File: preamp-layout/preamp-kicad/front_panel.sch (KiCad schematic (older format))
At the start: 30 parts, among them J16 Conn_01x03_Female, J17 Conn_01x03_Female, J18 Conn_01x03_Female, J19 Conn_01x03_Female, J20 Conn_01x03_Female, J21 Conn_01x03_Female, J22 Conn_01x03_Female, J23 Conn_01x03_Female, J24 Conn_01x05_Female, J25 Conn_01x02_Male, J26 Conn_01x02_Male, U4 MC33978

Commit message: Conn / Pin Updates
Updated cable headers, pin names, MCU conn layout. MCP4902 changeout for custom symbol.
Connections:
- net labels added: ~CS
- net labels removed: CS
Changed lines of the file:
@@
 CLK
 Text HLabel 6050 3400 0    50   Input ~ 0
-CS
+~CS
 Wire Wire Line
 	6050 3200 6200 3200
@@
 	1    0    0    -1
 $EndComp
-Text HLabel 9550 1650 0    50   Output ~ 0
+Text HLabel 9550 1750 0    50   Output ~ 0
 MISO
+Text HLabel 9550 1550 0    50   Input ~ 0
+CLK
+Text HLabel 9550 1650 0    50   Input ~ 0
+MOSI
 Text HLabel 9550 1450 0    50   Input ~ 0
-CLK
-Text HLabel 9550 1550 0    50   Input ~ 0
-MOSI
-Text HLabel 9550 1750 0    50   Input ~ 0
-CS
+~CS
 Text HLabel 9550 1850 0    50   Output ~ 0
 SW_INT

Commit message: I2C init commit
Changed design from using SPI interface to I2C interface, with exception of front LED array (SPI).
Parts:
- removed U4: MC33978, symbol preamp:MC33978
- added R122, R123, R124, R125, R70, R71: 1k, Resistor_SMD:R_1206_3216Metric_Pad1.42x1.75mm_HandSolder, symbol Device:R
- added SW10, SW11: Rotary_Encoder_Switch, symbol Device:Rotary_Encoder_Switch
- added U4: MCP23017_SO, Package_SO:SOIC-28W_7.5x17.9mm_P1.27mm, symbol Interface_Expansion:MCP23017_SO
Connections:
- net labels added: FP_INTA, FP_INTB, FP_SCL, FP_SDA, SEL_CLK, SEL_DT, SEL_SW, VOL_CLK, VOL_DT, VOL_SW, ~FP_RST
- net labels removed: CLK, MISO, MOSI, SW_INT, ~CS
- wire segments 122 -> 172
- no-connect marks 16 -> 2
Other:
- moved on the sheet: C17, C18, C19, C20, C21, C22, C23, C24, D12, J16, J17, J18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

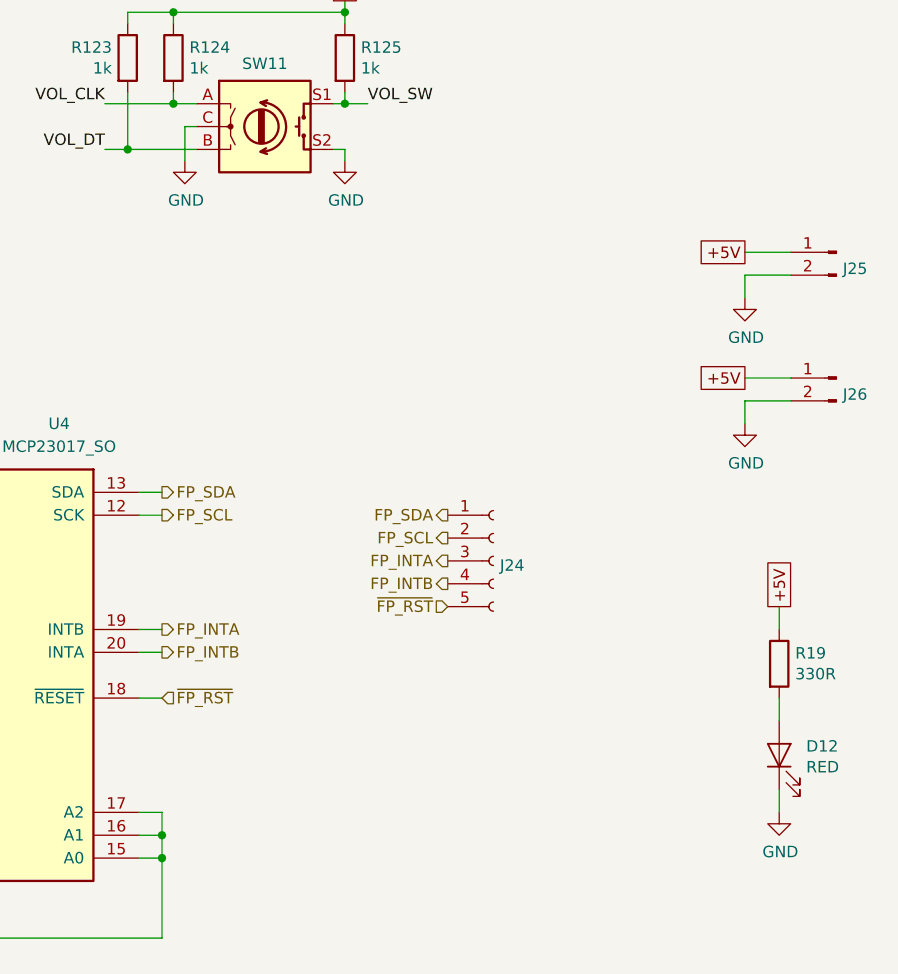
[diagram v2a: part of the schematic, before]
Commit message: Minor Updates
Moved headphone jack to amp pcb. I2C pin updates. Added caps to LED light strip. Added 0.1uF caps to all ICs.
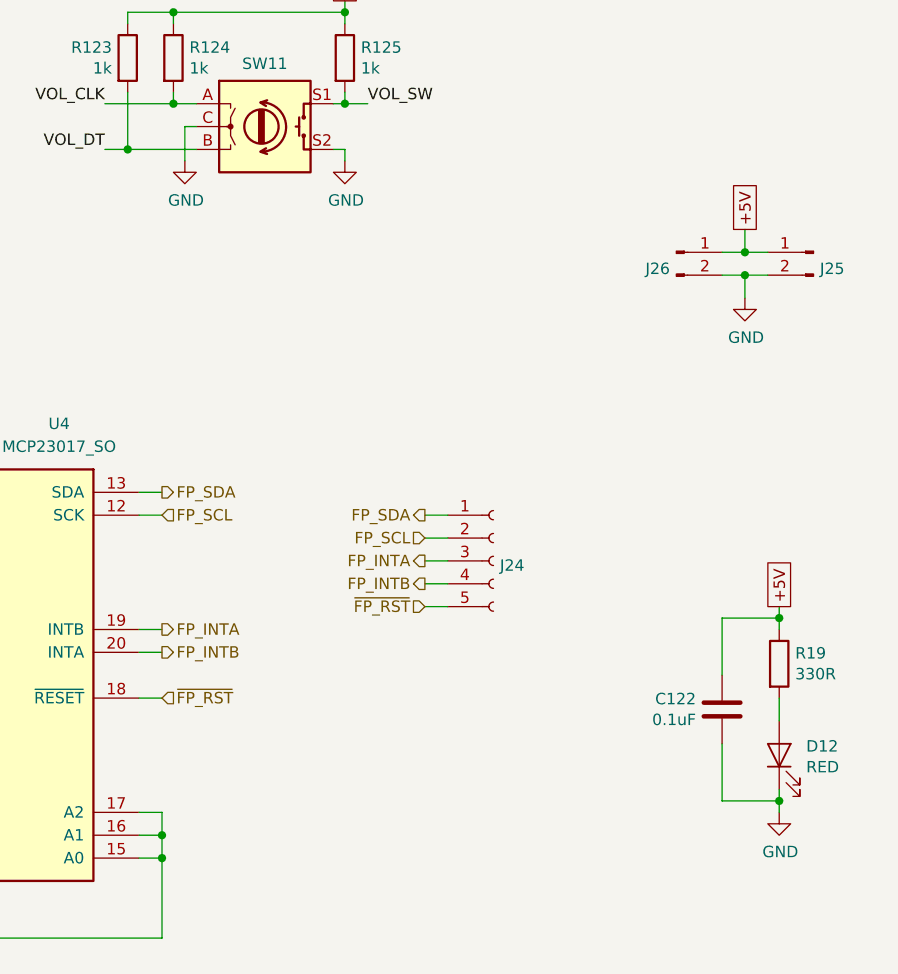
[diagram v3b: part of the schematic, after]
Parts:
- added C122: 0.1uF, Capacitor_SMD:C_0805_2012Metric_Pad1.15x1.40mm_HandSolder, symbol Device:C
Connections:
- net +5V: now also C122.1
- net GND: now also C122.2
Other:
- moved on the sheet: J25, J26
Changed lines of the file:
@@
 $Descr A4 11693 8268
 encoding utf-8
-Sheet 5 13
+Sheet 13 13
 Title "Front Panel"
 Date "2020-02-25"
@@
 $EndComp
 Wire Wire Line
-	10150 5050 10150 5150
+	10150 5050 10150 5100
 Wire Wire Line
 	10150 4650 10150 4750
 Wire Wire Line
-	10150 4250 10150 4350
+	10150 4250 10150 4300
 $Comp
 L Device:LED D?
@@
 L Connector:Conn_01x02_Male J?
 U 1 1 5E8B15E1
-P 10400 3250
+P 9700 2700
 AR Path="/5E5EF2D4/5E8B15E1" Ref="J?"  Part="1"
 AR Path="/6009D432/5E8B15E1" Ref="J?"  Part="1"
 AR Path="/5E5ECAAE/5E8B15E1" Ref="J26"  Part="1"
-F 0 "J26" H 10372 3178 50  0000 R CNN
-F 1 "Conn_01x02_Male" H 10372 3133 50  0001 R CNN
-F 2 "Connector_JST:JST_EH_B2B-EH-A_1x02_P2.50mm_Vertical" H 10400 3250 50  0001 C CNN
-F 3 "~" H 10400 3250 50  0001 C CNN
-	1    10400 3250
-	-1   0    0    -1
+F 0 "J26" H 9672 2628 50  0000 R CNN
+F 1 "Conn_01x02_Male" H 9672 2583 50  0001 R CNN
+F 2 "Connector_JST:JST_EH_B2B-EH-A_1x02_P2.50mm_Vertical" H 9700 2700 50  0001 C CNN
+F 3 "~" H 9700 2700 50  0001 C CNN
+	1    9700 2700
+	1    0    0    -1
 $EndComp
 $Comp
@@
 	1    0    0    -1
 $EndComp
-$Comp
-L power:GND #PWR?
-U 1 1 64EC55E1
-P 10000 3450
-AR Path="/5E26F6FE/64EC55E1" Ref="#PWR?"  Part="1"
-AR Path="/5E5ECAAE/64EC55E1" Ref="#PWR029"  Part="1"
-F 0 "#PWR029" H 10000 3200 50  0001 C CNN
-F 1 "GND" H 10005 3277 50  0000 C CNN
-F 2 "" H 10000 3450 50  0001 C CNN
-F 3 "" H 10000 3450 50  0001 C CNN
-	1    10000 3450
-	1    0    0    -1
-$EndComp
-Wire Wire Line
-	10200 3250 10000 3250
-Wire Wire Line
-	10000 3350 10000 3450
-Wire Wire Line
-	10200 3350 10000 3350
-Text GLabel 10000 3250 0    50   UnSpc ~ 0
-+5V
-Wire Wire Line
-	10200 2700 10000 2700
 Wire Wire Line
 	10000 2800 10000 2900
-Wire Wire Line
-	10200 2800 10000 2800
-Text GLabel 10000 2700 0    50   UnSpc ~ 0
+Text GLabel 10000 2600 1    50   UnSpc ~ 0
 +5V
 $Comp
 L Connector:Conn_01x02_Male J?
 U 1 1 60B80487
-P 10400 2700
+P 10300 2700
 AR Path="/5E5EF2D4/60B80487" Ref="J?"  Part="1"
 AR Path="/6009D432/60B80487" Ref="J?"  Part="1"
 AR Path="/5E5ECAAE/60B80487" Ref="J25"  Part="1"
-F 0 "J25" H 10372 2628 50  0000 R CNN
-F 1 "Conn_01x02_Male" H 10372 2583 50  0001 R CNN
-F 2 "Connector_JST:JST_EH_B2B-EH-A_1x02_P2.50mm_Vertical" H 10400 2700 50  0001 C CNN
-F 3 "~" H 10400 2700 50  0001 C CNN
-	1    10400 2700
+F 0 "J25" H 10272 2628 50  0000 R CNN
+F 1 "Conn_01x02_Male" H 10272 2583 50  0001 R CNN
+F 2 "Connector_JST:JST_EH_B2B-EH-A_1x02_P2.50mm_Vertical" H 10300 2700 50  0001 C CNN
+F 3 "~" H 10300 2700 50  0001 C CNN
+	1    10300 2700
 	-1   0    0    -1
 $EndComp
@@
 	6650 5650 6650 5700
 Wire Wire Line
-	6650 3350 6650 3450
-Wire Wire Line
 	7350 5150 7450 5150
 Wire Wire Line
@@
 	1    0    0    -1
 $EndComp
-Text HLabel 8700 4150 0    50   Output ~ 0
+Text HLabel 8600 4150 0    50   Output ~ 0
 FP_INTB
-Text HLabel 8700 3950 0    50   Output ~ 0
-FP_SCL
-Text HLabel 8700 4050 0    50   Output ~ 0
+Text HLabel 8600 4050 0    50   Output ~ 0
 FP_INTA
-Text HLabel 8700 3850 0    50   Output ~ 0
-FP_SDA
-Text HLabel 8700 4250 0    50   Input ~ 0
+Text HLabel 8600 4250 0    50   Input ~ 0
 ~FP_RST
 Text HLabel 7450 4450 2    50   Output ~ 0
 FP_INTB
-Text HLabel 7450 3850 2    50   Output ~ 0
+Text HLabel 7450 3850 2    50   Input ~ 0
 FP_SCL
 Text HLabel 7450 4350 2    50   Output ~ 0
@@
 Wire Wire Line
 	7350 4650 7450 4650
+Text HLabel 8600 3950 0    50   Input ~ 0
+FP_SCL
+Text HLabel 8600 3850 0    50   Output ~ 0
+FP_SDA
+Wire Wire Line
+	8600 3850 8700 3850
+Wire Wire Line
+	8600 3950 8700 3950
+Wire Wire Line
+	8600 4050 8700 4050
+Wire Wire Line
+	8600 4150 8700 4150
+Wire Wire Line
+	8600 4250 8700 4250
+Wire Wire Line
+	9900 2800 10000 2800
+Wire Wire Line
+	9900 2700 10000 2700
+Wire Wire Line
+	10100 2800 10000 2800
+Connection ~ 10000 2800
+Wire Wire Line
+	10000 2600 10000 2700
+Connection ~ 10000 2700
+Wire Wire Line
+	10000 2700 10100 2700
+Wire Wire Line
+	9900 4550 9900 4300
+Connection ~ 10150 4300
+Wire Wire Line
+	10150 4300 10150 4350
+Wire Wire Line
+	9900 4850 9900 5100
+Connection ~ 10150 5100
+Wire Wire Line
+	10150 5100 10150 5150
+Wire Wire Line
+	6650 3350 6650 3450
+$Comp
+L Device:C C?
+U 1 1 5E8C1B16
+P 9900 4700
+AR Path="/5E4A803E/5E8C1B16" Ref="C?"  Part="1"
+AR Path="/6009D432/5E8C1B16" Ref="C?"  Part="1"
+AR Path="/5E5ECAAE/5E8C1B16" Ref="C122"  Part="1"
+F 0 "C122" H 9786 4746 50  0000 R CNN
+F 1 "0.1uF" H 9786 4655 50  0000 R CNN
+F 2 "Capacitor_SMD:C_0805_2012Metric_Pad1.15x1.40mm_HandSolder" H 9938 4550 50  0001 C CNN
+F 3 "~" H 9900 4700 50  0001 C CNN
+	1    9900 4700
+	1    0    0    -1
+$EndComp
+Wire Wire Line
+	9900 4300 10150 4300
+Wire Wire Line
+	9900 5100 10150 5100
 $EndSCHEMATC

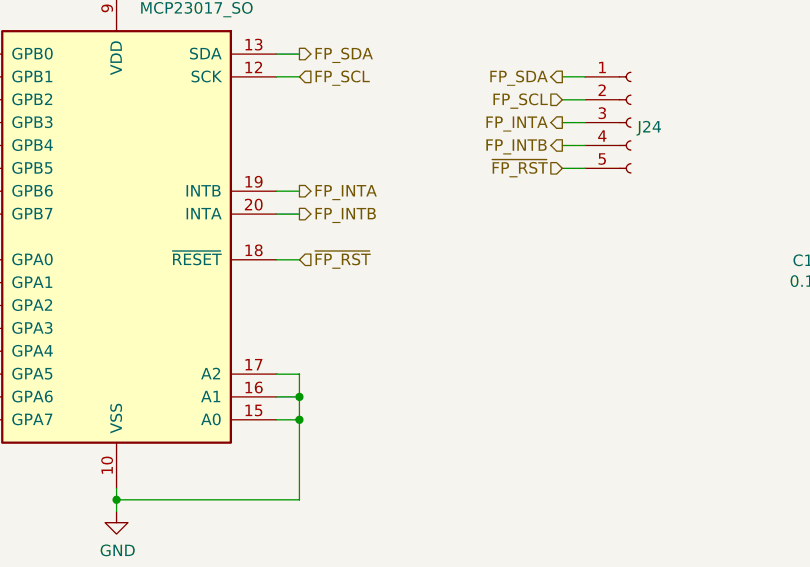
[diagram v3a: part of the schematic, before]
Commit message: Test branch combine (MCU changes)
Incorporated the changes made in the Test branch (can't stash using GitHub Desktop, I forgot to pull before I started making changes to the I2C thus the Test branch was created)

This includes adding an MCP23017 to the MCU board for IO expansion (flags), adding the pinouts for using an ESP8266 to the existing ESP32 pinout (so that either MCU could be used)
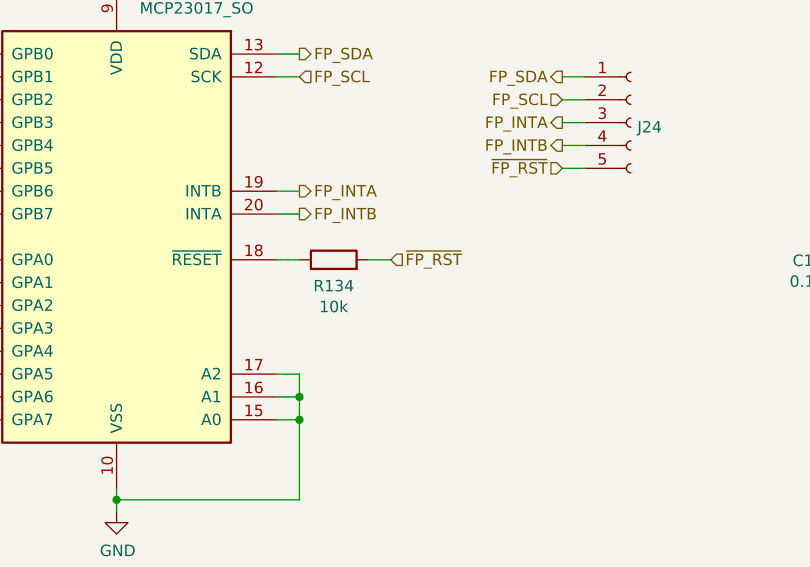
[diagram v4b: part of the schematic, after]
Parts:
- added R134: 10k, Resistor_SMD:R_1206_3216Metric_Pad1.42x1.75mm_HandSolder, symbol Device:R
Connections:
- net ~FP_RST: now also R134.2; no longer U4.18 (~RESET~)
- new net: R134.1, U4.18 (~RESET~)
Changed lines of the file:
@@
 Text HLabel 7450 3750 2    50   Output ~ 0
 FP_SDA
-Text HLabel 7450 4650 2    50   Input ~ 0
+Text HLabel 7850 4650 2    50   Input ~ 0
 ~FP_RST
 Wire Wire Line
@@
 	7350 4450 7450 4450
 Wire Wire Line
-	7350 4650 7450 4650
+	7750 4650 7850 4650
 Text HLabel 8600 3950 0    50   Input ~ 0
 FP_SCL
@@
 Wire Wire Line
 	9900 5100 10150 5100
+$Comp
+L Device:R R?
+U 1 1 60044E40
+P 7600 4650
+AR Path="/5E2D8DA2/60044E40" Ref="R?"  Part="1"
+AR Path="/60044E40" Ref="R?"  Part="1"
+AR Path="/5E27B612/60044E40" Ref="R?"  Part="1"
+AR Path="/5E5EF2D4/60044E40" Ref="R?"  Part="1"
+AR Path="/5E5ECAAE/60044E40" Ref="R134"  Part="1"
+F 0 "R134" V 7485 4650 50  0000 C CNN
+F 1 "10k" V 7394 4650 50  0000 C CNN
+F 2 "Resistor_SMD:R_1206_3216Metric_Pad1.42x1.75mm_HandSolder" V 7530 4650 50  0001 C CNN
+F 3 "~" H 7600 4650 50  0001 C CNN
+	1    7600 4650
+	0    -1   -1   0
+$EndComp
+Wire Wire Line
+	7350 4650 7450 4650
 $EndSCHEMATC

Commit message: RefDes Update
Re-ran refdes assignment, updated BOM accordingly.
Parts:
- added R133, R135: 1.5k, Resistor_SMD:R_1206_3216Metric_Pad1.42x1.75mm_HandSolder, symbol Device:R
- renumbered C17 to C114, C18 to C115, C19 to C116, C20 to C117, C21 to C118, C22 to C119, C23 to C120, C24 to C121, D12 to D60, J16 to J74, J17 to J75, J18 to J76, J19 to J77, J20 to J78, J21 to J79, J22 to J80, J23 to J81, J26 to J82, J25 to J83, J24 to J84, R11 to R121, R12 to R122, R13 to R123, R14 to R124, R15 to R125, R16 to R126, R17 to R127, R18 to R128, R19 to R129, R70 to R130, R71 to R131, R122 to R132, R123 to R136, R124 to R137, R125 to R138, SW10 to SW11, SW11 to SW12, U4 to U23
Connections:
- net +5V: now also R133.1, R135.1
- net FP_SCL: now also R135.2
- net FP_SDA: now also R133.2
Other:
- moved on the sheet: C122, D60, J82, J83, J84, R129, R130, R131, R132, R134, R136, R137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

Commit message: PCB layout
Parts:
- removed J82, J83: Conn_01x02_Male, Connector_JST:JST_EH_B2B-EH-A_1x02_P2.50mm_Vertical, symbol Connector:Conn_01x02_Male
- added J54, J55: Conn_01x04_Male, Connector_JST:JST_EH_S4B-EH_1x04_P2.50mm_Horizontal, symbol Connector:Conn_01x04_Male
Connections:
- net +5V: now also J54.4 (Pin_4), J55.4 (Pin_4)
- net GND: now also J54.3 (Pin_3), J55.3 (Pin_3)
- new net +15V: J54.1 (Pin_1), J55.1 (Pin_1)
- new net -15V: J54.2 (Pin_2), J55.2 (Pin_2)
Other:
- moved on the sheet: C122, D60, R129
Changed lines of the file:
@@
 L Device:R R?
 U 1 1 5ECB89C1
-P 4900 6700
+P 4600 6700
 AR Path="/5E2D8DA2/5ECB89C1" Ref="R?"  Part="1"
 AR Path="/5ECB89C1" Ref="R?"  Part="1"
@@
 AR Path="/5E5EF2D4/5ECB89C1" Ref="R?"  Part="1"
 AR Path="/5E5ECAAE/5ECB89C1" Ref="R129"  Part="1"
-F 0 "R129" H 4970 6746 50  0000 L CNN
-F 1 "330R" H 4970 6655 50  0000 L CNN
-F 2 "Resistor_SMD:R_1206_3216Metric_Pad1.42x1.75mm_HandSolder" V 4830 6700 50  0001 C CNN
-F 3 "~" H 4900 6700 50  0001 C CNN
-	1    4900 6700
-	1    0    0    -1
-$EndComp
-Text GLabel 4900 6450 1    50   UnSpc ~ 0
+F 0 "R129" H 4670 6746 50  0000 L CNN
+F 1 "330R" H 4670 6655 50  0000 L CNN
+F 2 "Resistor_SMD:R_1206_3216Metric_Pad1.42x1.75mm_HandSolder" V 4530 6700 50  0001 C CNN
+F 3 "~" H 4600 6700 50  0001 C CNN
+	1    4600 6700
+	1    0    0    -1
+$EndComp
+Text GLabel 4600 6450 1    50   UnSpc ~ 0
 +5V
 $Comp
 L power:GND #PWR?
 U 1 1 5ECB89D0
-P 4900 7350
+P 4600 7350
 AR Path="/5E26F6FE/5ECB89D0" Ref="#PWR?"  Part="1"
 AR Path="/5E5EF2D4/5ECB89D0" Ref="#PWR?"  Part="1"
 AR Path="/5E5ECAAE/5ECB89D0" Ref="#PWR0132"  Part="1"
-F 0 "#PWR0132" H 4900 7100 50  0001 C CNN
-F 1 "GND" H 4905 7177 50  0000 C CNN
-F 2 "" H 4900 7350 50  0001 C CNN
-F 3 "" H 4900 7350 50  0001 C CNN
-	1    4900 7350
-	1    0    0    -1
-$EndComp
-Wire Wire Line
-	4900 7250 4900 7300
-Wire Wire Line
-	4900 6850 4900 6950
-Wire Wire Line
-	4900 6450 4900 6500
+F 0 "#PWR0132" H 4600 7100 50  0001 C CNN
+F 1 "GND" H 4605 7177 50  0000 C CNN
+F 2 "" H 4600 7350 50  0001 C CNN
+F 3 "" H 4600 7350 50  0001 C CNN
+	1    4600 7350
+	1    0    0    -1
+$EndComp
+Wire Wire Line
+	4600 7250 4600 7300
+Wire Wire Line
+	4600 6850 4600 6950
+Wire Wire Line
+	4600 6450 4600 6500
 $Comp
 L Device:LED D?
 U 1 1 5ECB89C7
-P 4900 7100
+P 4600 7100
 AR Path="/5E2D8DA2/5ECB89C7" Ref="D?"  Part="1"
 AR Path="/5E27B612/5ECB89C7" Ref="D?"  Part="1"
 AR Path="/5E5EF2D4/5ECB89C7" Ref="D?"  Part="1"
 AR Path="/5E5ECAAE/5ECB89C7" Ref="D60"  Part="1"
-F 0 "D60" V 4939 6982 50  0000 R CNN
-F 1 "RED" V 4848 6982 50  0000 R CNN
-F 2 "LED_SMD:LED_1206_3216Metric_Pad1.42x1.75mm_HandSolder" H 4900 7100 50  0001 C CNN
-F 3 "~" H 4900 7100 50  0001 C CNN
-	1    4900 7100
+F 0 "D60" V 4639 6982 50  0000 R CNN
+F 1 "RED" V 4548 6982 50  0000 R CNN
+F 2 "LED_SMD:LED_1206_3216Metric_Pad1.42x1.75mm_HandSolder" H 4600 7100 50  0001 C CNN
+F 3 "~" H 4600 7100 50  0001 C CNN
+	1    4600 7100
 	0    -1   -1   0
 $EndComp
@@
 	9700 4650 9600 4650
 Wire Wire Line
-	4650 6750 4650 6500
-Connection ~ 4900 6500
-Wire Wire Line
-	4900 6500 4900 6550
-Wire Wire Line
-	4650 7050 4650 7300
-Connection ~ 4900 7300
-Wire Wire Line
-	4900 7300 4900 7350
+	4350 6750 4350 6500
+Connection ~ 4600 6500
+Wire Wire Line
+	4600 6500 4600 6550
+Wire Wire Line
+	4350 7050 4350 7300
+Connection ~ 4600 7300
+Wire Wire Line
+	4600 7300 4600 7350
 $Comp
 L Device:C C?
 U 1 1 5E8C1B16
-P 4650 6900
+P 4350 6900
 AR Path="/5E4A803E/5E8C1B16" Ref="C?"  Part="1"
 AR Path="/6009D432/5E8C1B16" Ref="C?"  Part="1"
 AR Path="/5E5ECAAE/5E8C1B16" Ref="C122"  Part="1"
-F 0 "C122" H 4536 6946 50  0000 R CNN
-F 1 "0.1uF" H 4536 6855 50  0000 R CNN
-F 2 "Capacitor_SMD:C_0805_2012Metric_Pad1.15x1.40mm_HandSolder" H 4688 6750 50  0001 C CNN
-F 3 "~" H 4650 6900 50  0001 C CNN
-	1    4650 6900
-	1    0    0    -1
-$EndComp
-Wire Wire Line
-	4650 6500 4900 6500
-Wire Wire Line
-	4650 7300 4900 7300
+F 0 "C122" H 4236 6946 50  0000 R CNN
+F 1 "0.1uF" H 4236 6855 50  0000 R CNN
+F 2 "Capacitor_SMD:C_0805_2012Metric_Pad1.15x1.40mm_HandSolder" H 4388 6750 50  0001 C CNN
+F 3 "~" H 4350 6900 50  0001 C CNN
+	1    4350 6900
+	1    0    0    -1
+$EndComp
+Wire Wire Line
+	4350 6500 4600 6500
+Wire Wire Line
+	4350 7300 4600 7300
 $Comp
 L Device:R R?
@@
 Wire Wire Line
 	7800 3250 7950 3250
-Wire Wire Line
-	5850 6950 5950 6950
-Connection ~ 5850 6950
-Wire Wire Line
-	5850 6850 5850 6950
-Connection ~ 5850 7050
-Wire Wire Line
-	5950 7050 5850 7050
-Wire Wire Line
-	5750 6950 5850 6950
-Wire Wire Line
-	5750 7050 5850 7050
-$Comp
-L Connector:Conn_01x02_Male J?
-U 1 1 60B80487
-P 6150 6950
-AR Path="/5E5EF2D4/60B80487" Ref="J?"  Part="1"
-AR Path="/6009D432/60B80487" Ref="J?"  Part="1"
-AR Path="/5E5ECAAE/60B80487" Ref="J83"  Part="1"
-F 0 "J83" H 6122 6878 50  0000 R CNN
-F 1 "Conn_01x02_Male" H 6122 6833 50  0001 R CNN
-F 2 "Connector_JST:JST_EH_B2B-EH-A_1x02_P2.50mm_Vertical" H 6150 6950 50  0001 C CNN
-F 3 "~" H 6150 6950 50  0001 C CNN
-	1    6150 6950
+$Comp
+L Connector:Conn_01x04_Male J?
+U 1 1 5FCE2A06
+P 5150 6850
+AR Path="/5E2D8DA2/5FCE2A06" Ref="J?"  Part="1"
+AR Path="/5E5ECAAE/5FCE2A06" Ref="J54"  Part="1"
+F 0 "J54" H 5258 7039 50  0000 C CNN
+F 1 "Conn_01x04_Male" H 5258 7040 50  0001 C CNN
+F 2 "Connector_JST:JST_EH_S4B-EH_1x04_P2.50mm_Horizontal" H 5150 6850 50  0001 C CNN
+F 3 "~" H 5150 6850 50  0001 C CNN
+	1    5150 6850
+	1    0    0    -1
+$EndComp
+$Comp
+L Connector:Conn_01x04_Male J?
+U 1 1 5FCE2A0C
+P 6400 6850
+AR Path="/5E2D8DA2/5FCE2A0C" Ref="J?"  Part="1"
+AR Path="/5E5ECAAE/5FCE2A0C" Ref="J55"  Part="1"
+F 0 "J55" H 6372 6778 50  0000 R CNN
+F 1 "Conn_01x04_Male" H 6508 7040 50  0001 C CNN
+F 2 "Connector_JST:JST_EH_S4B-EH_1x04_P2.50mm_Horizontal" H 6400 6850 50  0001 C CNN
+F 3 "~" H 6400 6850 50  0001 C CNN
+	1    6400 6850
 	-1   0    0    -1
 $EndComp
-Text GLabel 5850 6850 1    50   UnSpc ~ 0
+Wire Wire Line
+	5350 6750 5650 6750
+Wire Wire Line
+	5350 6850 5950 6850
+Text GLabel 5650 6650 1    50   UnSpc ~ 0
++15V
+Wire Wire Line
+	5650 6650 5650 6750
+Connection ~ 5650 6750
+Text GLabel 5950 6650 1    50   UnSpc ~ 0
+-15V
+Wire Wire Line
+	5950 7150 5950 7050
+Text GLabel 5950 7150 3    50   UnSpc ~ 0
 +5V
-Wire Wire Line
-	5850 7050 5850 7150
+Connection ~ 5950 7050
+Wire Wire Line
+	5950 7050 6200 7050
+Wire Wire Line
+	5650 6750 6200 6750
+Wire Wire Line
+	5350 7050 5950 7050
+Wire Wire Line
+	5350 6950 5650 6950
 $Comp
 L power:GND #PWR?
-U 1 1 64EC680F
-P 5850 7150
-AR Path="/5E26F6FE/64EC680F" Ref="#PWR?"  Part="1"
-AR Path="/5E5ECAAE/64EC680F" Ref="#PWR0133"  Part="1"
-F 0 "#PWR0133" H 5850 6900 50  0001 C CNN
-F 1 "GND" H 5855 6977 50  0000 C CNN
-F 2 "" H 5850 7150 50  0001 C CNN
-F 3 "" H 5850 7150 50  0001 C CNN
-	1    5850 7150
-	1    0    0    -1
-$EndComp
-$Comp
-L Connector:Conn_01x02_Male J?
-U 1 1 5E8B15E1
-P 5550 6950
-AR Path="/5E5EF2D4/5E8B15E1" Ref="J?"  Part="1"
-AR Path="/6009D432/5E8B15E1" Ref="J?"  Part="1"
-AR Path="/5E5ECAAE/5E8B15E1" Ref="J82"  Part="1"
-F 0 "J82" H 5522 6878 50  0000 R CNN
-F 1 "Conn_01x02_Male" H 5522 6833 50  0001 R CNN
-F 2 "Connector_JST:JST_EH_B2B-EH-A_1x02_P2.50mm_Vertical" H 5550 6950 50  0001 C CNN
-F 3 "~" H 5550 6950 50  0001 C CNN
-	1    5550 6950
-	1    0    0    -1
-$EndComp
+U 1 1 5FCE2A1F
+P 5650 7150
+AR Path="/6009D432/5FCE2A1F" Ref="#PWR?"  Part="1"
+AR Path="/5E2D8DA2/5FCE2A1F" Ref="#PWR?"  Part="1"
+AR Path="/5E5ECAAE/5FCE2A1F" Ref="#PWR048"  Part="1"
+F 0 "#PWR048" H 5650 6900 50  0001 C CNN
+F 1 "GND" H 5655 6977 50  0000 C CNN
+F 2 "" H 5650 7150 50  0001 C CNN
+F 3 "" H 5650 7150 50  0001 C CNN
+	1    5650 7150
+	1    0    0    -1
+$EndComp
+Wire Wire Line
+	5650 7150 5650 6950
+Connection ~ 5650 6950
+Wire Wire Line
+	5650 6950 6200 6950
+Wire Wire Line
+	5950 6650 5950 6850
+Connection ~ 5950 6850
+Wire Wire Line
+	5950 6850 6200 6850
 $EndSCHEMATC
